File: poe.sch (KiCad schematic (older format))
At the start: 25 parts, among them IC1 TPS2378DDA

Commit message: Add test points
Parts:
- added TP? (x6): TP_SMD1MM, antmicro-footprints:Testpoint_smd_1mm, symbol antmicroTestPoints:TP_SMD1MM
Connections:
- no-connect marks 1 -> 0
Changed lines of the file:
@@
 Wire Wire Line
 	5775 4625 7400 4625
-NoConn ~ 6750 5075
 Text GLabel 2475 5475 0    50   Input ~ 0
 PAIR78
@@
 	1    0    0    -1
 $EndComp
-Wire Wire Line
-	10225 4175 10675 4175
 Wire Wire Line
 	10675 4825 10675 4175
@@
 Text Notes 8475 5825 0    50   ~ 0
 PSE must see draw of ~~10mA to maintain PoE.\nPDQE30-D draws 8~~15mA with no load\nThis circuit provides exrta ~~3mA and indicates VDD presence
+$Comp
+L antmicroTestPoints:TP_SMD1MM TP?
+U 1 1 62405733
+P 4850 4525
+F 0 "TP?" H 4850 4430 50  0000 C CNN
+F 1 "TP_SMD1MM" H 4850 4425 50  0001 C CNN
+F 2 "antmicro-footprints:Testpoint_smd_1mm" H 5050 4725 60  0001 L CNN
+F 3 "" H 5050 4825 60  0001 L CNN
+	1    4850 4525
+	-1   0    0    1
+$EndComp
+$Comp
+L antmicroTestPoints:TP_SMD1MM TP?
+U 1 1 624090F9
+P 10675 4075
+F 0 "TP?" H 10625 4122 50  0000 R CNN
+F 1 "TP_SMD1MM" H 10675 3975 50  0001 C CNN
+F 2 "antmicro-footprints:Testpoint_smd_1mm" H 10875 4275 60  0001 L CNN
+F 3 "" H 10875 4375 60  0001 L CNN
+	1    10675 4075
+	-1   0    0    1
+$EndComp
+Wire Wire Line
+	10225 4175 10675 4175
+Connection ~ 10675 4175
+$Comp
+L antmicroTestPoints:TP_SMD1MM TP?
+U 1 1 62413367
+P 13125 4525
+F 0 "TP?" H 13125 4430 50  0000 C CNN
+F 1 "TP_SMD1MM" H 13125 4425 50  0001 C CNN
+F 2 "antmicro-footprints:Testpoint_smd_1mm" H 13325 4725 60  0001 L CNN
+F 3 "" H 13325 4825 60  0001 L CNN
+	1    13125 4525
+	-1   0    0    1
+$EndComp
+$Comp
+L antmicroTestPoints:TP_SMD1MM TP?
+U 1 1 62416240
+P 13125 5125
+F 0 "TP?" H 13125 5030 50  0000 C CNN
+F 1 "TP_SMD1MM" H 13125 5025 50  0001 C CNN
+F 2 "antmicro-footprints:Testpoint_smd_1mm" H 13325 5325 60  0001 L CNN
+F 3 "" H 13325 5425 60  0001 L CNN
+	1    13125 5125
+	1    0    0    -1
+$EndComp
+$Comp
+L antmicroTestPoints:TP_SMD1MM TP?
+U 1 1 62420B0C
+P 4850 5875
+F 0 "TP?" H 4850 5780 50  0000 C CNN
+F 1 "TP_SMD1MM" H 4850 5775 50  0001 C CNN
+F 2 "antmicro-footprints:Testpoint_smd_1mm" H 5050 6075 60  0001 L CNN
+F 3 "" H 5050 6175 60  0001 L CNN
+	1    4850 5875
+	1    0    0    -1
+$EndComp
+$Comp
+L antmicroTestPoints:TP_SMD1MM TP?
+U 1 1 624298A6
+P 6850 5075
+F 0 "TP?" V 6850 5025 50  0000 R CNN
+F 1 "TP_SMD1MM" H 6850 4975 50  0001 C CNN
+F 2 "antmicro-footprints:Testpoint_smd_1mm" H 7050 5275 60  0001 L CNN
+F 3 "" H 7050 5375 60  0001 L CNN
+	1    6850 5075
+	0    -1   -1   0
+$EndComp
 $EndSCHEMATC

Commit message: Annotate test points, reimport 510R from global library
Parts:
- gave numbers to parts that had none: 6
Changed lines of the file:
@@
 PSE must see draw of ~~10mA to maintain PoE.\nPDQE30-D draws 8~~15mA with no load\nThis circuit provides exrta ~~3mA and indicates VDD presence
 $Comp
-L antmicroTestPoints:TP_SMD1MM TP?
+L antmicroTestPoints:TP_SMD1MM TP69
 U 1 1 62405733
 P 4850 4525
-F 0 "TP?" H 4850 4430 50  0000 C CNN
+F 0 "TP69" H 4850 4430 50  0000 C CNN
 F 1 "TP_SMD1MM" H 4850 4425 50  0001 C CNN
 F 2 "antmicro-footprints:Testpoint_smd_1mm" H 5050 4725 60  0001 L CNN
@@
 $EndComp
 $Comp
-L antmicroTestPoints:TP_SMD1MM TP?
+L antmicroTestPoints:TP_SMD1MM TP72
 U 1 1 624090F9
 P 10675 4075
-F 0 "TP?" H 10625 4122 50  0000 R CNN
+F 0 "TP72" H 10625 4122 50  0000 R CNN
 F 1 "TP_SMD1MM" H 10675 3975 50  0001 C CNN
 F 2 "antmicro-footprints:Testpoint_smd_1mm" H 10875 4275 60  0001 L CNN
@@
 Connection ~ 10675 4175
 $Comp
-L antmicroTestPoints:TP_SMD1MM TP?
+L antmicroTestPoints:TP_SMD1MM TP73
 U 1 1 62413367
 P 13125 4525
-F 0 "TP?" H 13125 4430 50  0000 C CNN
+F 0 "TP73" H 13125 4430 50  0000 C CNN
 F 1 "TP_SMD1MM" H 13125 4425 50  0001 C CNN
 F 2 "antmicro-footprints:Testpoint_smd_1mm" H 13325 4725 60  0001 L CNN
@@
 $EndComp
 $Comp
-L antmicroTestPoints:TP_SMD1MM TP?
+L antmicroTestPoints:TP_SMD1MM TP74
 U 1 1 62416240
 P 13125 5125
-F 0 "TP?" H 13125 5030 50  0000 C CNN
+F 0 "TP74" H 13125 5030 50  0000 C CNN
 F 1 "TP_SMD1MM" H 13125 5025 50  0001 C CNN
 F 2 "antmicro-footprints:Testpoint_smd_1mm" H 13325 5325 60  0001 L CNN
@@
 $EndComp
 $Comp
-L antmicroTestPoints:TP_SMD1MM TP?
+L antmicroTestPoints:TP_SMD1MM TP70
 U 1 1 62420B0C
 P 4850 5875
-F 0 "TP?" H 4850 5780 50  0000 C CNN
+F 0 "TP70" H 4850 5780 50  0000 C CNN
 F 1 "TP_SMD1MM" H 4850 5775 50  0001 C CNN
 F 2 "antmicro-footprints:Testpoint_smd_1mm" H 5050 6075 60  0001 L CNN
@@
 $EndComp
 $Comp
-L antmicroTestPoints:TP_SMD1MM TP?
+L antmicroTestPoints:TP_SMD1MM TP71
 U 1 1 624298A6
 P 6850 5075
-F 0 "TP?" V 6850 5025 50  0000 R CNN
+F 0 "TP71" V 6850 5025 50  0000 R CNN
 F 1 "TP_SMD1MM" H 6850 4975 50  0001 C CNN
 F 2 "antmicro-footprints:Testpoint_smd_1mm" H 7050 5275 60  0001 L CNN

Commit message: Loclib
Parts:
- TP69, TP70, TP71, TP72, TP73, TP74: footprint antmicro-footprints:Testpoint_smd_1mm -> sa800u-baseboard-hw-footprints:Testpoint_smd_1mm; symbol antmicroTestPoints:TP_SMD1MM -> sa800u-baseboard-hw:TP_SMD1MM
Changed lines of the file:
@@
 PSE must see draw of ~~10mA to maintain PoE.\nPDQE30-D draws 8~~15mA with no load\nThis circuit provides exrta ~~3mA and indicates VDD presence
 $Comp
-L antmicroTestPoints:TP_SMD1MM TP69
+L sa800u-baseboard-hw:TP_SMD1MM TP69
 U 1 1 62405733
 P 4850 4525
 F 0 "TP69" H 4850 4430 50  0000 C CNN
 F 1 "TP_SMD1MM" H 4850 4425 50  0001 C CNN
-F 2 "antmicro-footprints:Testpoint_smd_1mm" H 5050 4725 60  0001 L CNN
+F 2 "sa800u-baseboard-hw-footprints:Testpoint_smd_1mm" H 5050 4725 60  0001 L CNN
 F 3 "" H 5050 4825 60  0001 L CNN
 	1    4850 4525
@@
 $EndComp
 $Comp
-L antmicroTestPoints:TP_SMD1MM TP72
+L sa800u-baseboard-hw:TP_SMD1MM TP72
 U 1 1 624090F9
 P 10675 4075
 F 0 "TP72" H 10625 4122 50  0000 R CNN
 F 1 "TP_SMD1MM" H 10675 3975 50  0001 C CNN
-F 2 "antmicro-footprints:Testpoint_smd_1mm" H 10875 4275 60  0001 L CNN
+F 2 "sa800u-baseboard-hw-footprints:Testpoint_smd_1mm" H 10875 4275 60  0001 L CNN
 F 3 "" H 10875 4375 60  0001 L CNN
 	1    10675 4075
@@
 Connection ~ 10675 4175
 $Comp
-L antmicroTestPoints:TP_SMD1MM TP73
+L sa800u-baseboard-hw:TP_SMD1MM TP73
 U 1 1 62413367
 P 13125 4525
 F 0 "TP73" H 13125 4430 50  0000 C CNN
 F 1 "TP_SMD1MM" H 13125 4425 50  0001 C CNN
-F 2 "antmicro-footprints:Testpoint_smd_1mm" H 13325 4725 60  0001 L CNN
+F 2 "sa800u-baseboard-hw-footprints:Testpoint_smd_1mm" H 13325 4725 60  0001 L CNN
 F 3 "" H 13325 4825 60  0001 L CNN
 	1    13125 4525
@@
 $EndComp
 $Comp
-L antmicroTestPoints:TP_SMD1MM TP74
+L sa800u-baseboard-hw:TP_SMD1MM TP74
 U 1 1 62416240
 P 13125 5125
 F 0 "TP74" H 13125 5030 50  0000 C CNN
 F 1 "TP_SMD1MM" H 13125 5025 50  0001 C CNN
-F 2 "antmicro-footprints:Testpoint_smd_1mm" H 13325 5325 60  0001 L CNN
+F 2 "sa800u-baseboard-hw-footprints:Testpoint_smd_1mm" H 13325 5325 60  0001 L CNN
 F 3 "" H 13325 5425 60  0001 L CNN
 	1    13125 5125
@@
 $EndComp
 $Comp
-L antmicroTestPoints:TP_SMD1MM TP70
+L sa800u-baseboard-hw:TP_SMD1MM TP70
 U 1 1 62420B0C
 P 4850 5875
 F 0 "TP70" H 4850 5780 50  0000 C CNN
 F 1 "TP_SMD1MM" H 4850 5775 50  0001 C CNN
-F 2 "antmicro-footprints:Testpoint_smd_1mm" H 5050 6075 60  0001 L CNN
+F 2 "sa800u-baseboard-hw-footprints:Testpoint_smd_1mm" H 5050 6075 60  0001 L CNN
 F 3 "" H 5050 6175 60  0001 L CNN
 	1    4850 5875
@@
 $EndComp
 $Comp
-L antmicroTestPoints:TP_SMD1MM TP71
+L sa800u-baseboard-hw:TP_SMD1MM TP71
 U 1 1 624298A6
 P 6850 5075
 F 0 "TP71" V 6850 5025 50  0000 R CNN
 F 1 "TP_SMD1MM" H 6850 4975 50  0001 C CNN
-F 2 "antmicro-footprints:Testpoint_smd_1mm" H 7050 5275 60  0001 L CNN
+F 2 "sa800u-baseboard-hw-footprints:Testpoint_smd_1mm" H 7050 5275 60  0001 L CNN
 F 3 "" H 7050 5375 60  0001 L CNN
 	1    6850 5075

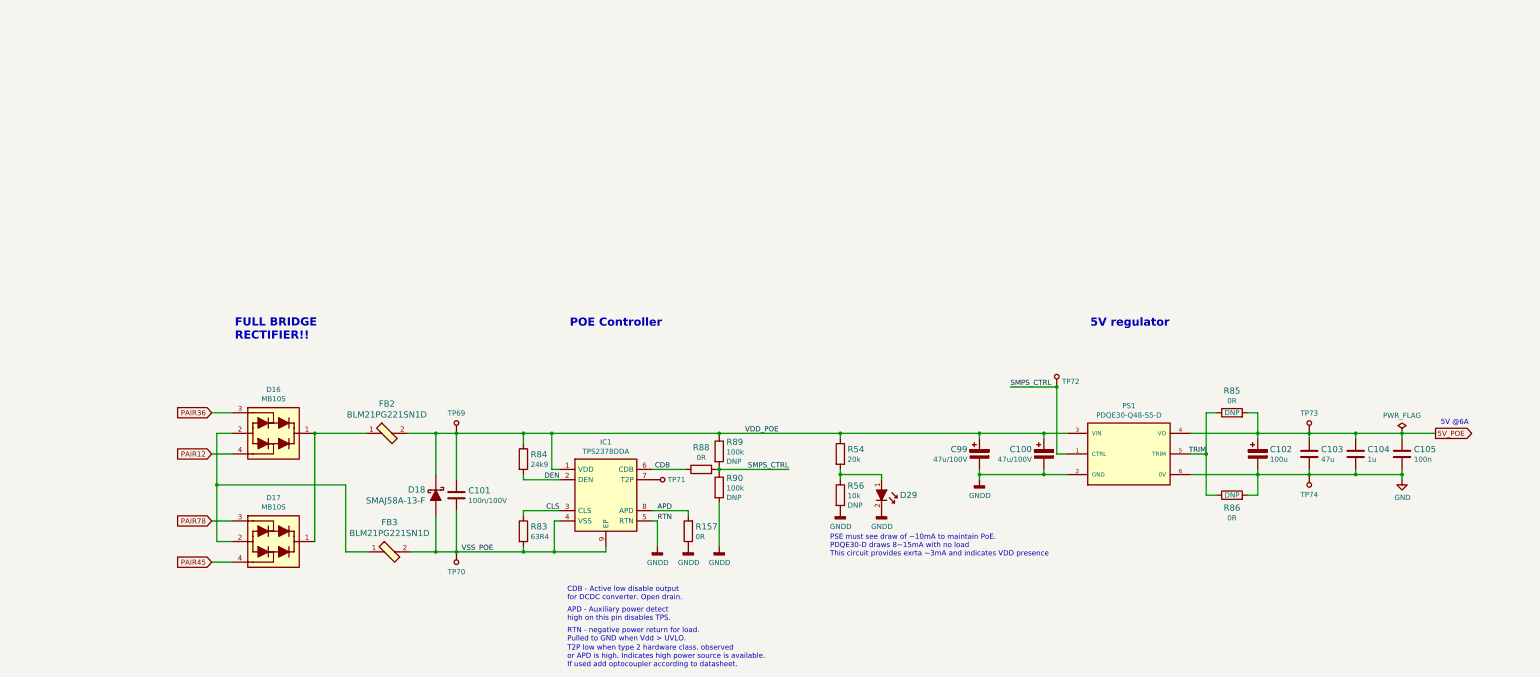
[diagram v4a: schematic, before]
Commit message: Reorganize schematics, add descriptions in top left corner
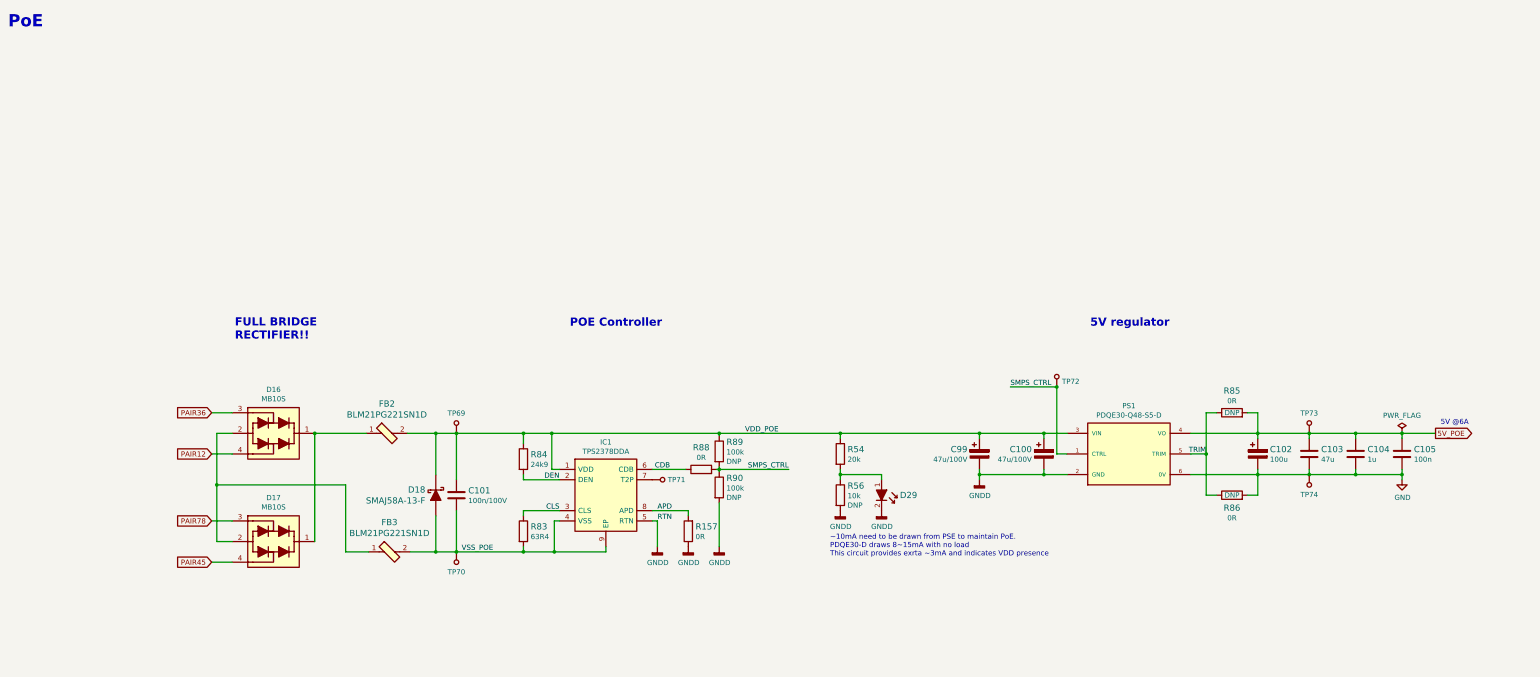
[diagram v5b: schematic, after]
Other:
- note added: "PoE"
- note added: "~~10mA need to be drawn from PSE to maintain PoE.\nPDQE30-D draws 8~~15mA with no load\nThis circuit provides exrta ~~3mA and indicates VDD presence"
- note removed: "APD - Auxiliary power detect \nhigh on this pin disables TPS."
- note removed: "CDB - Active low disable output \nfor DCDC converter. Open drain."
- note removed: "PSE must see draw of ~~10mA to maintain PoE.\nPDQE30-D draws 8~~15mA with no load\nThis circuit provides exrta ~~3mA and indicates VDD presence"
- note removed: "RTN - negative power return for load.\nPulled to GND when Vdd > UVLO."
- note removed: "T2P low when type 2 hardware class. observed\nor APD is high. Indicates high power source is available. \nIf used add optocoupler according to datasheet."
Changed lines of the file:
@@
 	1    0    0    -1
 $EndComp
-Text Notes 5925 6250 0    50   ~ 0
-CDB - Active low disable output \nfor DCDC converter. Open drain.
 $Comp
 L sa800u-baseboard-hw:GNDD #PWR0152
@@
 	1    0    0    -1
 $EndComp
-Text Notes 5925 6450 0    50   ~ 0
-APD - Auxiliary power detect \nhigh on this pin disables TPS.
-Text Notes 5925 6650 0    50   ~ 0
-RTN - negative power return for load.\nPulled to GND when Vdd > UVLO.
-Text Notes 5925 6900 0    50   ~ 0
-T2P low when type 2 hardware class. observed\nor APD is high. Indicates high power source is available. \nIf used add optocoupler according to datasheet.
 Text Label 6800 5475 0    50   ~ 0
 RTN
@@
 Wire Wire Line
 	8575 4625 9925 4625
-Text Notes 8475 5825 0    50   ~ 0
-PSE must see draw of ~~10mA to maintain PoE.\nPDQE30-D draws 8~~15mA with no load\nThis circuit provides exrta ~~3mA and indicates VDD presence
 $Comp
 L sa800u-baseboard-hw:TP_SMD1MM TP69
@@
 	0    -1   -1   0
 $EndComp
+Text Notes 500  700  0    118  ~ 24
+PoE
+Text Notes 8475 5825 0    50   ~ 0
+~~10mA need to be drawn from PSE to maintain PoE.\nPDQE30-D draws 8~~15mA with no load\nThis circuit provides exrta ~~3mA and indicates VDD presence
 $EndSCHEMATC
